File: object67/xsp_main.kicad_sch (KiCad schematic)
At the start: 0 parts

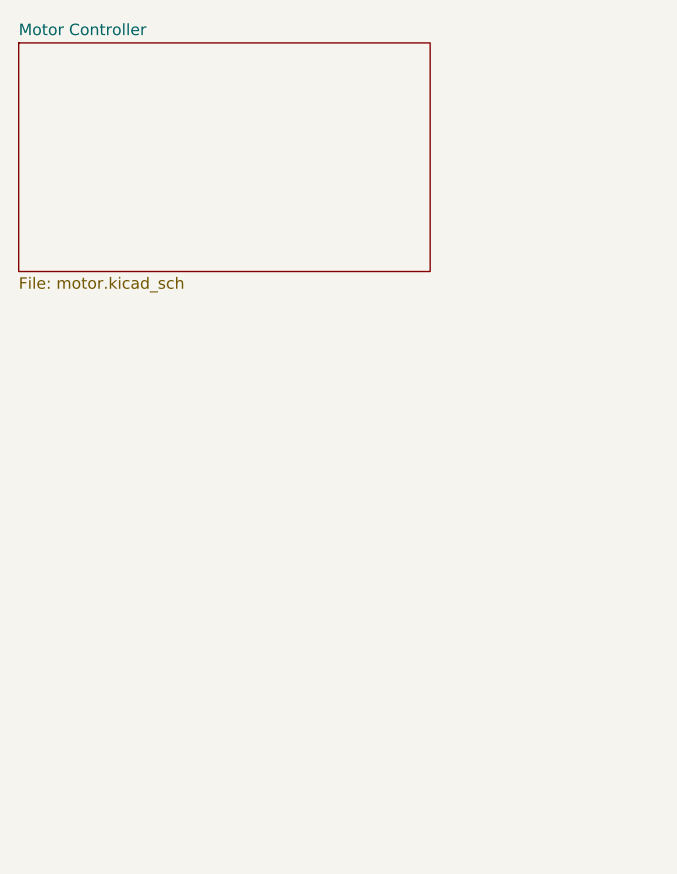
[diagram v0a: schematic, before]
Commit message: Finished schematic for DAC
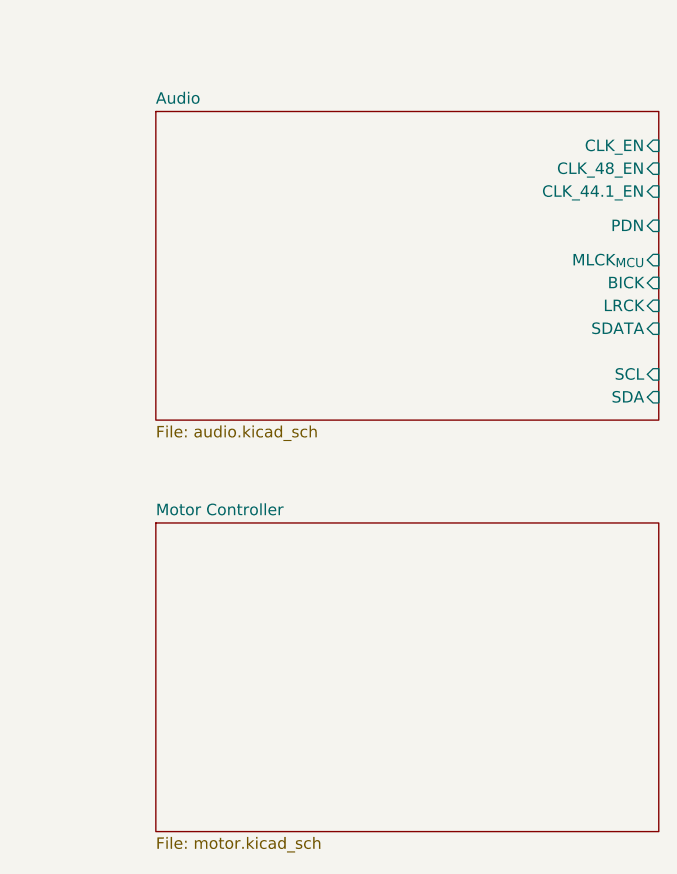
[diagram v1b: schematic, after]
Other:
- added sheet Audio (audio.kicad_sch)
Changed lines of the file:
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@@
 	(paper "A4")
 	(sheet
-		(at 63.5 46.99)
-		(size 45.72 25.4)
+		(at 78.74 100.33)
+		(size 55.88 34.29)
 		(exclude_from_sim no)
 		(in_bom yes)
@@
 		)
 		(property "Sheetname" "Motor Controller"
-			(at 63.5 46.2784 0)
+			(at 78.74 99.6184 0)
 			(effects
 				(font
@@
 		)
 		(property "Sheetfile" "motor.kicad_sch"
-			(at 63.5 72.9746 0)
+			(at 78.74 135.2046 0)
 			(effects
 				(font
@@
 				)
 			)
+		)
+	)
+	(sheet
+		(at 78.74 54.61)
+		(size 55.88 34.29)
+		(exclude_from_sim no)
+		(in_bom yes)
+		(on_board yes)
+		(dnp no)
+		(fields_autoplaced yes)
+		(stroke
+			(width 0.1524)
+			(type solid)
+		)
+		(fill
+			(color 0 0 0 0.0000)
+		)
+		(property "Sheetname" "Audio"
+			(at 78.74 53.8984 0)
+			(effects
+				(font
+					(size 1.27 1.27)
+				)
+				(justify left bottom)
+			)
+		)
+		(property "Sheetfile" "audio.kicad_sch"
+			(at 78.74 89.4846 0)
+			(effects
+				(font
+					(size 1.27 1.27)
+				)
+				(justify left top)
+			)
+		)
+		(pin "BICK" input
+			(at 134.62 73.66 0)
+			(effects
+				(font
+					(size 1.27 1.27)
+				)
+				(justify right)
+			)
+		)
+		(pin "CLK_44.1_EN" input
+			(at 134.62 63.5 0)
+			(effects
+				(font
+					(size 1.27 1.27)
+				)
+				(justify right)
+			)
+		)
+		(pin "CLK_48_EN" input
+			(at 134.62 60.96 0)
+			(effects
+				(font
+					(size 1.27 1.27)
+				)
+				(justify right)
+			)
+		)
+		(pin "CLK_EN" input
+			(at 134.62 58.42 0)
+			(effects
+				(font
+					(size 1.27 1.27)
+				)
+				(justify right)
+			)
+		)
+		(pin "LRCK" input
+			(at 134.62 76.2 0)
+			(effects
+				(font
+					(size 1.27 1.27)
+				)
+				(justify right)
+			)
+		)
+		(pin "MLCK_{MCU}" input
+			(at 134.62 71.12 0)
+			(effects
+				(font
+					(size 1.27 1.27)
+				)
+				(justify right)
+			)
+		)
+		(pin "PDN" input
+			(at 134.62 67.31 0)
+			(effects
+				(font
+					(size 1.27 1.27)
+				)
+				(justify right)
+			)
+		)
+		(pin "SCL" input
+			(at 134.62 83.82 0)
+			(effects
+				(font
+					(size 1.27 1.27)
+				)
+				(justify right)
+			)
+		)
+		(pin "SDA" input
+			(at 134.62 86.36 0)
+			(effects
+				(font
+					(size 1.27 1.27)
+				)
+				(justify right)
+			)
+		)
+		(pin "SDATA" input
+			(at 134.62 78.74 0)
+			(effects
+				(font
+					(size 1.27 1.27)
+				)
+				(justify right)
+			)
+		)
+		(instances
+			(project "object67"
+				(path "/a52a93a9-ab60-414c-847b-3047ce4056cf/2d7be8e2-05a1-49f5-8994-604be09973f2"
+					(page "4")
+				)
+			)

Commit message: Changes
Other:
- added sheet Analog Frontend (frontend.kicad_sch)
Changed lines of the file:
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@@
+				)
+			)
+			(project "xsp_main"
+				(path "/bff3f72a-b367-4d17-84b1-aae8062d5933"
+					(page "3")
+				)
+			)
+		)
+	)
+	(sheet
+		(at 175.26 53.34)
+		(size 55.88 36.83)
+		(exclude_from_sim no)
+		(in_bom yes)
+		(on_board yes)
+		(dnp no)
+		(fields_autoplaced yes)
+		(stroke
+			(width 0.1524)
+			(type solid)
+		)
+		(fill
+			(color 0 0 0 0.0000)
+		)
+		(property "Sheetname" "Analog Frontend"
+			(at 175.26 52.6284 0)
+			(effects
+				(font
+					(size 1.27 1.27)
+				)
+				(justify left bottom)
+			)
+		)
+		(property "Sheetfile" "frontend.kicad_sch"
+			(at 175.26 90.7546 0)
+			(effects
+				(font
+					(size 1.27 1.27)
+				)
+				(justify left top)
+			)
+		)
+		(instances
+			(project "object67"
+				(path "/a52a93a9-ab60-414c-847b-3047ce4056cf/2d7be8e2-05a1-49f5-8994-604be09973f2"
+					(page "5")
+				)
+			)
+			(project "xsp_main"
+				(path "/bff3f72a-b367-4d17-84b1-aae8062d5933"
+					(page "4")
 				)
 			)
@@
 				)
 			)
+			(project "xsp_main"
+				(path "/bff3f72a-b367-4d17-84b1-aae8062d5933"
+					(page "2")
+				)
+			)
 		)
 	)
+	(sheet_instances
+		(path "/"
+			(page "1")
+		)
+	)
+	(embedded_fonts no)
 )

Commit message: Analog frontend
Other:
- sheet Audio ports: added AOUTLN, AOUTLP, AOUTRN, AOUTRP, Audio_{IN}LN, Audio_{IN}LP, Audio_{IN}RN, Audio_{IN}RP, BICK_{ADC}, BICK_{DAC}, GPO_{ADC}, LRCK_{ADC}, LRCK_{DAC}, SDATA_{ADC}, SDATA_{DAC}; removed BICK, LRCK, SDATA
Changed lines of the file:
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@@
 	)
 	(sheet
-		(at 78.74 54.61)
-		(size 55.88 34.29)
+		(at 73.66 36.83)
+		(size 66.04 54.61)
 		(exclude_from_sim no)
 		(in_bom yes)
@@
 		)
 		(property "Sheetname" "Audio"
-			(at 78.74 53.8984 0)
+			(at 73.66 36.1184 0)
 			(effects
 				(font
@@
 		)
 		(property "Sheetfile" "audio.kicad_sch"
-			(at 78.74 89.4846 0)
+			(at 73.66 92.0246 0)
 			(effects
 				(font
@@
 			)
 		)
-		(pin "BICK" input
-			(at 134.62 73.66 0)
-			(effects
-				(font
-					(size 1.27 1.27)
-				)
-				(justify right)
-			)
-		)
 		(pin "CLK_44.1_EN" input
-			(at 134.62 63.5 0)
+			(at 139.7 45.72 0)
 			(effects
 				(font
@@
 		)
 		(pin "CLK_48_EN" input
-			(at 134.62 60.96 0)
+			(at 139.7 43.18 0)
 			(effects
 				(font
@@
 		)
 		(pin "CLK_EN" input
-			(at 134.62 58.42 0)
-			(effects
-				(font
-					(size 1.27 1.27)
-				)
-				(justify right)
-			)
-		)
-		(pin "LRCK" input
-			(at 134.62 76.2 0)
+			(at 139.7 40.64 0)
 			(effects
 				(font
@@
 		)
 		(pin "MLCK_{MCU}" input
-			(at 134.62 71.12 0)
+			(at 139.7 53.34 0)
 			(effects
 				(font
@@
 		)
 		(pin "PDN" input
-			(at 134.62 67.31 0)
+			(at 139.7 49.53 0)
 			(effects
 				(font
@@
 		)
 		(pin "SCL" input
-			(at 134.62 83.82 0)
+			(at 139.7 64.77 0)
 			(effects
 				(font
@@
 		)
 		(pin "SDA" input
-			(at 134.62 86.36 0)
-			(effects
-				(font
-					(size 1.27 1.27)
-				)
-				(justify right)
-			)
-		)
-		(pin "SDATA" input
-			(at 134.62 78.74 0)
-			(effects
-				(font
-					(size 1.27 1.27)
-				)
-				(justify right)
-			)
-		)
+			(at 139.7 67.31 0)
+			(effects
+				(font
+					(size 1.27 1.27)
+				)
+				(justify right)
+			)
+		)
+		(pin "AOUTLN" input
+			(at 139.7 71.12 0)
+			(effects
+				(font
+					(size 1.27 1.27)
+				)
+				(justify right)
+			)
+		)
+		(pin "AOUTLP" input
+			(at 139.7 73.66 0)
+			(effects
+				(font
+					(size 1.27 1.27)
+				)
+				(justify right)
+			)
+		)
+		(pin "AOUTRN" input
+			(at 139.7 76.2 0)
+			(effects
+				(font
+					(size 1.27 1.27)
+				)
+				(justify right)
+			)
+		)
+		(pin "AOUTRP" input
+			(at 139.7 78.74 0)
+			(effects
+				(font
+					(size 1.27 1.27)
+				)
+				(justify right)
+			)
+		)
+		(pin "Audio_{IN}LN" input
+			(at 73.66 43.18 180)
+			(effects
+				(font
+					(size 1.27 1.27)
+				)
+				(justify left)
+			)
+		)
+		(pin "Audio_{IN}LP" input
+			(at 73.66 45.72 180)
+			(effects
+				(font
+					(size 1.27 1.27)
+				)
+				(justify left)
+			)
+		)
+		(pin "Audio_{IN}RN" input
+			(at 73.66 50.8 180)
+			(effects
+				(font
+					(size 1.27 1.27)
+				)
+				(justify left)
+			)
+		)
+		(pin "Audio_{IN}RP" input
+			(at 73.66 53.34 180)
+			(effects
+				(font
+					(size 1.27 1.27)
+				)
+				(justify left)
+			)
+		)
+		(pin "BICK_{ADC}" input
+			(at 73.66 57.15 180)
+			(effects
+				(font
+					(size 1.27 1.27)
+				)
+				(justify left)
+			)
+		)
+		(pin "BICK_{DAC}" input
+			(at 73.66 59.69 180)
+			(effects
+				(font
+					(size 1.27 1.27)
+				)
+				(justify left)
+			)
+		)
+		(pin "GPO_{ADC}" input
+			(at 73.66 62.23 180)
+			(effects
+				(font
+					(size 1.27 1.27)
+				)
+				(justify left)
+			)
+		)
+		(pin "LRCK_{ADC}" input
+			(at 73.66 64.77 180)
+			(effects
+				(font
+					(size 1.27 1.27)
+				)
+				(justify left)
+			)
+		)
+		(pin "LRCK_{DAC}" input
+			(at 73.66 67.31 180)
+			(effects
+				(font
+					(size 1.27 1.27)
+				)
+				(justify left)
+			)
+		)
+		(pin "SDATA_{ADC}" input
+			(at 73.66 69.85 180)
+			(effects
+				(font
+					(size 1.27 1.27)
+				)
+				(justify left)
+			)
+		)
+		(pin "SDATA_{DAC}" input
+			(at 73.66 72.39 180)
+			(effects
+				(font
+					(size 1.27 1.27)
+				)
+				(justify left)
+			)
+		)

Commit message: KiCad crashed x2
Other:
- sheet Audio ports: added none; removed AOUTLN, AOUTLP, AOUTRN, AOUTRP, Audio_{IN}LN, Audio_{IN}LP, Audio_{IN}RN, Audio_{IN}RP, BICK_{ADC}, BICK_{DAC}, CLK_44.1_EN, CLK_48_EN, CLK_EN, GPO_{ADC}, LRCK_{ADC}, LRCK_{DAC}, MLCK_{MCU}, PDN, SCL, SDA, SDATA_{ADC}, SDATA_{DAC}
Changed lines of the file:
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@@
-			)
-		)
-		(pin "CLK_44.1_EN" input
-			(at 139.7 45.72 0)
-			(effects
-				(font
-					(size 1.27 1.27)
-				)
-				(justify right)
-			)
-		)
-		(pin "CLK_48_EN" input
-			(at 139.7 43.18 0)
-			(effects
-				(font
-					(size 1.27 1.27)
-				)
-				(justify right)
-			)
-		)
-		(pin "CLK_EN" input
-			(at 139.7 40.64 0)
-			(effects
-				(font
-					(size 1.27 1.27)
-				)
-				(justify right)
-			)
-		)
-		(pin "MLCK_{MCU}" input
-			(at 139.7 53.34 0)
-			(effects
-				(font
-					(size 1.27 1.27)
-				)
-				(justify right)
-			)
-		)
-		(pin "PDN" input
-			(at 139.7 49.53 0)
-			(effects
-				(font
-					(size 1.27 1.27)
-				)
-				(justify right)
-			)
-		)
-		(pin "SCL" input
-			(at 139.7 64.77 0)
-			(effects
-				(font
-					(size 1.27 1.27)
-				)
-				(justify right)
-			)
-		)
-		(pin "SDA" input
-			(at 139.7 67.31 0)
-			(effects
-				(font
-					(size 1.27 1.27)
-				)
-				(justify right)
-			)
-		)
-		(pin "AOUTLN" input
-			(at 139.7 71.12 0)
-			(effects
-				(font
-					(size 1.27 1.27)
-				)
-				(justify right)
-			)
-		)
-		(pin "AOUTLP" input
-			(at 139.7 73.66 0)
-			(effects
-				(font
-					(size 1.27 1.27)
-				)
-				(justify right)
-			)
-		)
-		(pin "AOUTRN" input
-			(at 139.7 76.2 0)
-			(effects
-				(font
-					(size 1.27 1.27)
-				)
-				(justify right)
-			)
-		)
-		(pin "AOUTRP" input
-			(at 139.7 78.74 0)
-			(effects
-				(font
-					(size 1.27 1.27)
-				)
-				(justify right)
-			)
-		)
-		(pin "Audio_{IN}LN" input
-			(at 73.66 43.18 180)
-			(effects
-				(font
-					(size 1.27 1.27)
-				)
-				(justify left)
-			)
-		)
-		(pin "Audio_{IN}LP" input
-			(at 73.66 45.72 180)
-			(effects
-				(font
-					(size 1.27 1.27)
-				)
-				(justify left)
-			)
-		)
-		(pin "Audio_{IN}RN" input
-			(at 73.66 50.8 180)
-			(effects
-				(font
-					(size 1.27 1.27)
-				)
-				(justify left)
-			)
-		)
-		(pin "Audio_{IN}RP" input
-			(at 73.66 53.34 180)
-			(effects
-				(font
-					(size 1.27 1.27)
-				)
-				(justify left)
-			)
-		)
-		(pin "BICK_{ADC}" input
-			(at 73.66 57.15 180)
-			(effects
-				(font
-					(size 1.27 1.27)
-				)
-				(justify left)
-			)
-		)
-		(pin "BICK_{DAC}" input
-			(at 73.66 59.69 180)
-			(effects
-				(font
-					(size 1.27 1.27)
-				)
-				(justify left)
-			)
-		)
-		(pin "GPO_{ADC}" input
-			(at 73.66 62.23 180)
-			(effects
-				(font
-					(size 1.27 1.27)
-				)
-				(justify left)
-			)
-		)
-		(pin "LRCK_{ADC}" input
-			(at 73.66 64.77 180)
-			(effects
-				(font
-					(size 1.27 1.27)
-				)
-				(justify left)
-			)
-		)
-		(pin "LRCK_{DAC}" input
-			(at 73.66 67.31 180)
-			(effects
-				(font
-					(size 1.27 1.27)
-				)
-				(justify left)
-			)
-		)
-		(pin "SDATA_{ADC}" input
-			(at 73.66 69.85 180)
-			(effects
-				(font
-					(size 1.27 1.27)
-				)
-				(justify left)
-			)
-		)
-		(pin "SDATA_{DAC}" input
-			(at 73.66 72.39 180)
-			(effects
-				(font
-					(size 1.27 1.27)
-				)
-				(justify left)
 			)
 		)

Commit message: ????
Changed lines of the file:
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@@
 	(paper "A4")
 	(sheet
-		(at 78.74 100.33)
+		(at 205.74 118.11)
 		(size 55.88 34.29)
 		(exclude_from_sim no)
@@
 		)
 		(property "Sheetname" "Motor Controller"
-			(at 78.74 99.6184 0)
+			(at 205.74 117.3984 0)
 			(effects
 				(font
@@
 		)
 		(property "Sheetfile" "motor.kicad_sch"
-			(at 78.74 135.2046 0)
+			(at 205.74 152.9846 0)
 			(effects
 				(font
@@
 	)
 	(sheet
-		(at 175.26 53.34)
+		(at 204.47 71.12)
 		(size 55.88 36.83)
 		(exclude_from_sim no)
@@
 		)
 		(property "Sheetname" "Analog Frontend"
-			(at 175.26 52.6284 0)
+			(at 204.47 70.4084 0)
 			(effects
 				(font
@@
 		)
 		(property "Sheetfile" "frontend.kicad_sch"
-			(at 175.26 90.7546 0)
+			(at 204.47 108.5346 0)
 			(effects
 				(font
@@
 	)
 	(sheet
-		(at 73.66 36.83)
-		(size 66.04 54.61)
+		(at 205.74 22.86)
+		(size 58.42 38.1)
 		(exclude_from_sim no)
 		(in_bom yes)
@@
 		)
 		(property "Sheetname" "Audio"
-			(at 73.66 36.1184 0)
+			(at 205.74 22.1484 0)
 			(effects
 				(font
@@
 		)
 		(property "Sheetfile" "audio.kicad_sch"
-			(at 73.66 92.0246 0)
+			(at 205.74 61.5446 0)
 			(effects
 				(font
